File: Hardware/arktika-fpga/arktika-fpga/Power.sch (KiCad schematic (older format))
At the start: 40 parts

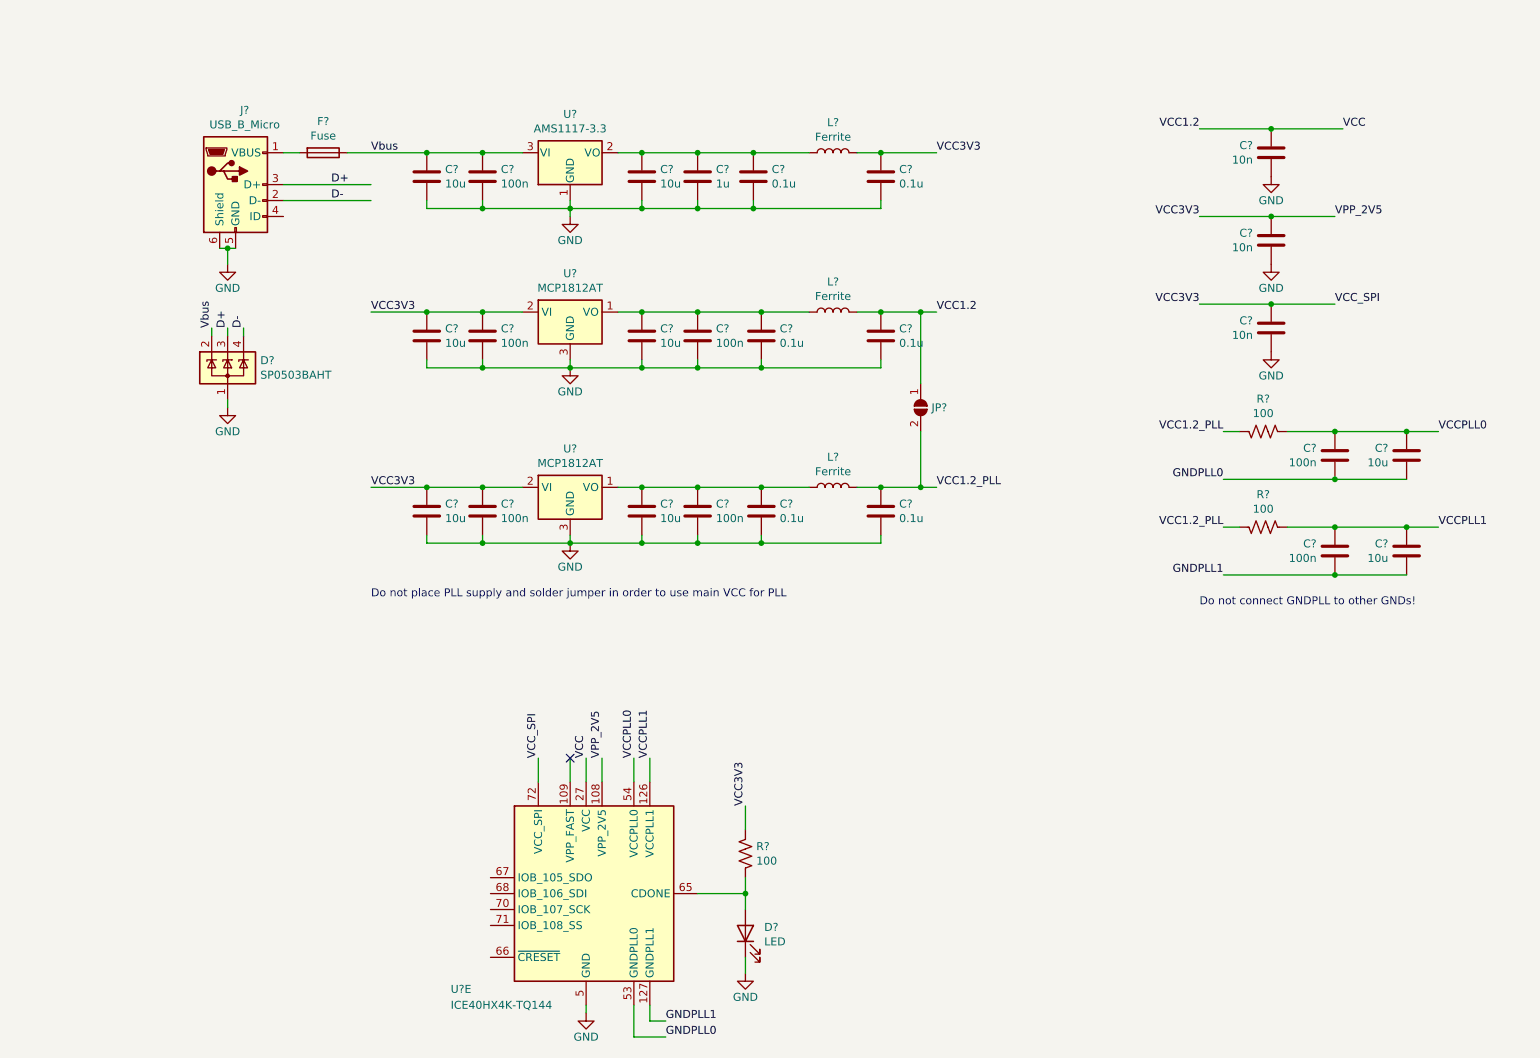
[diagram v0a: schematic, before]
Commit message: Started doing usb and programming
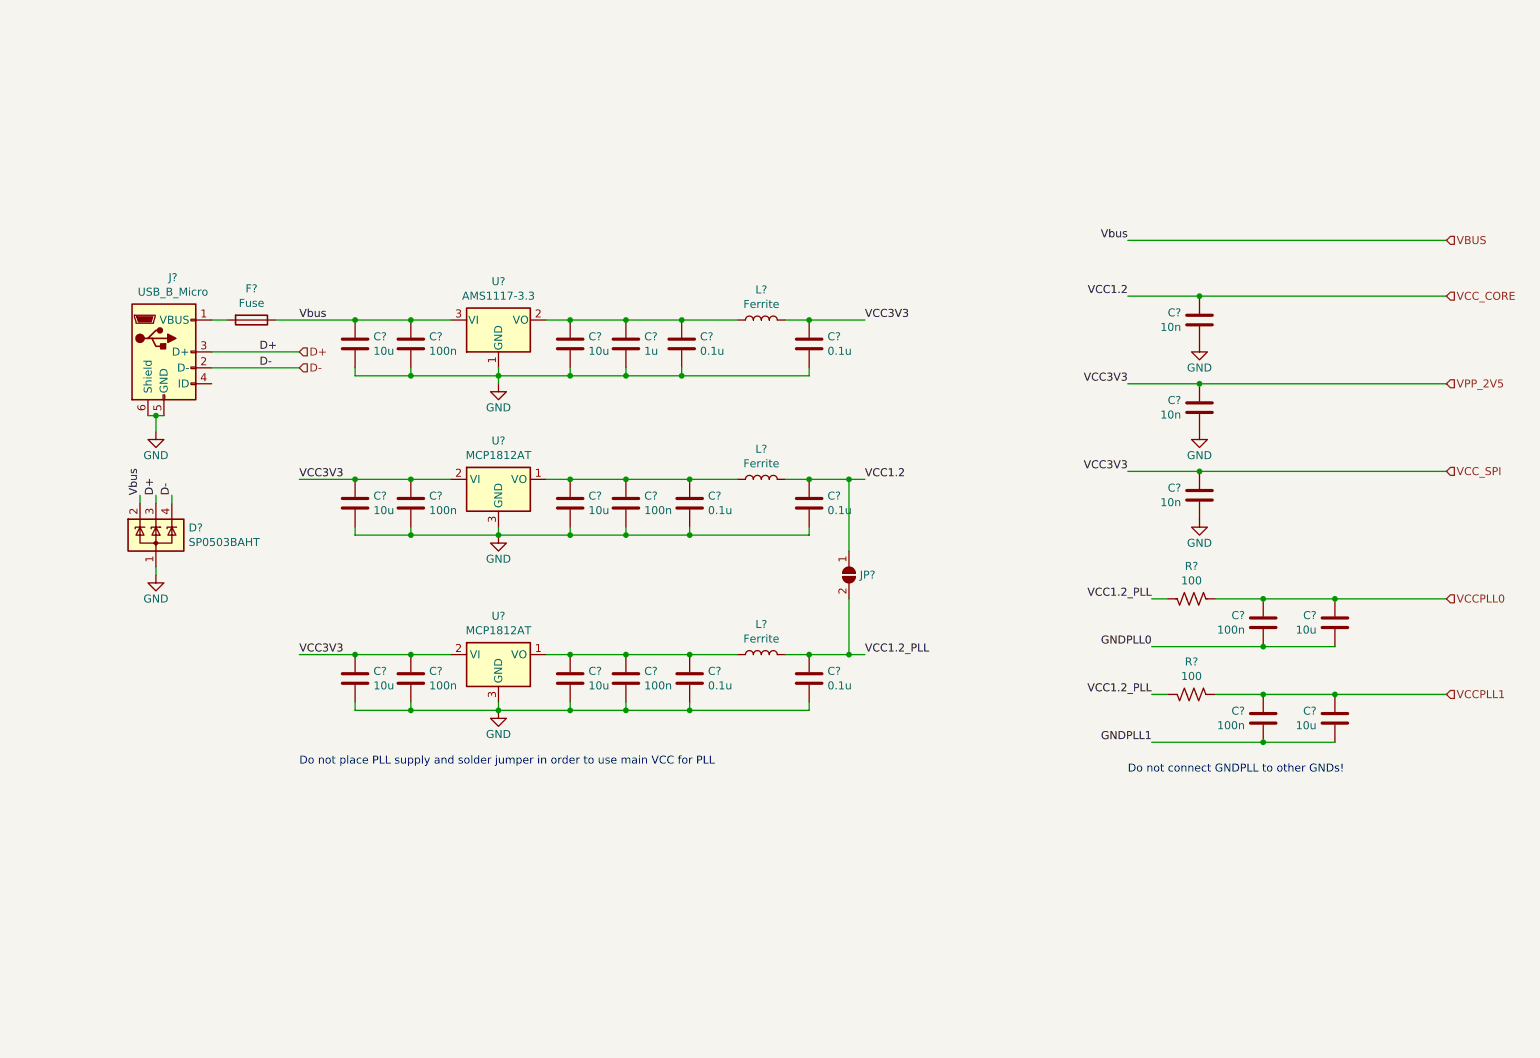
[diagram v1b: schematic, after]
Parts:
- removed D?: LED, symbol Device:LED
- removed R?: 100, symbol Device:R_US
- removed U?: ICE40HX4K-TQ144, Package_QFP:TQFP-144_20x20mm_P0.5mm, symbol FPGA_Lattice:ICE40HX4K-TQ144
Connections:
- net VCC renamed VCC_CORE
- net VCC3V3 renamed VCC_SPI
- net Vbus renamed VBUS
- no-connect marks 1 -> 0
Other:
- moved on the sheet: C?, D?, F?, J?, JP?, L?, R?, U?

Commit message: Added designators, some io, and some peripherals
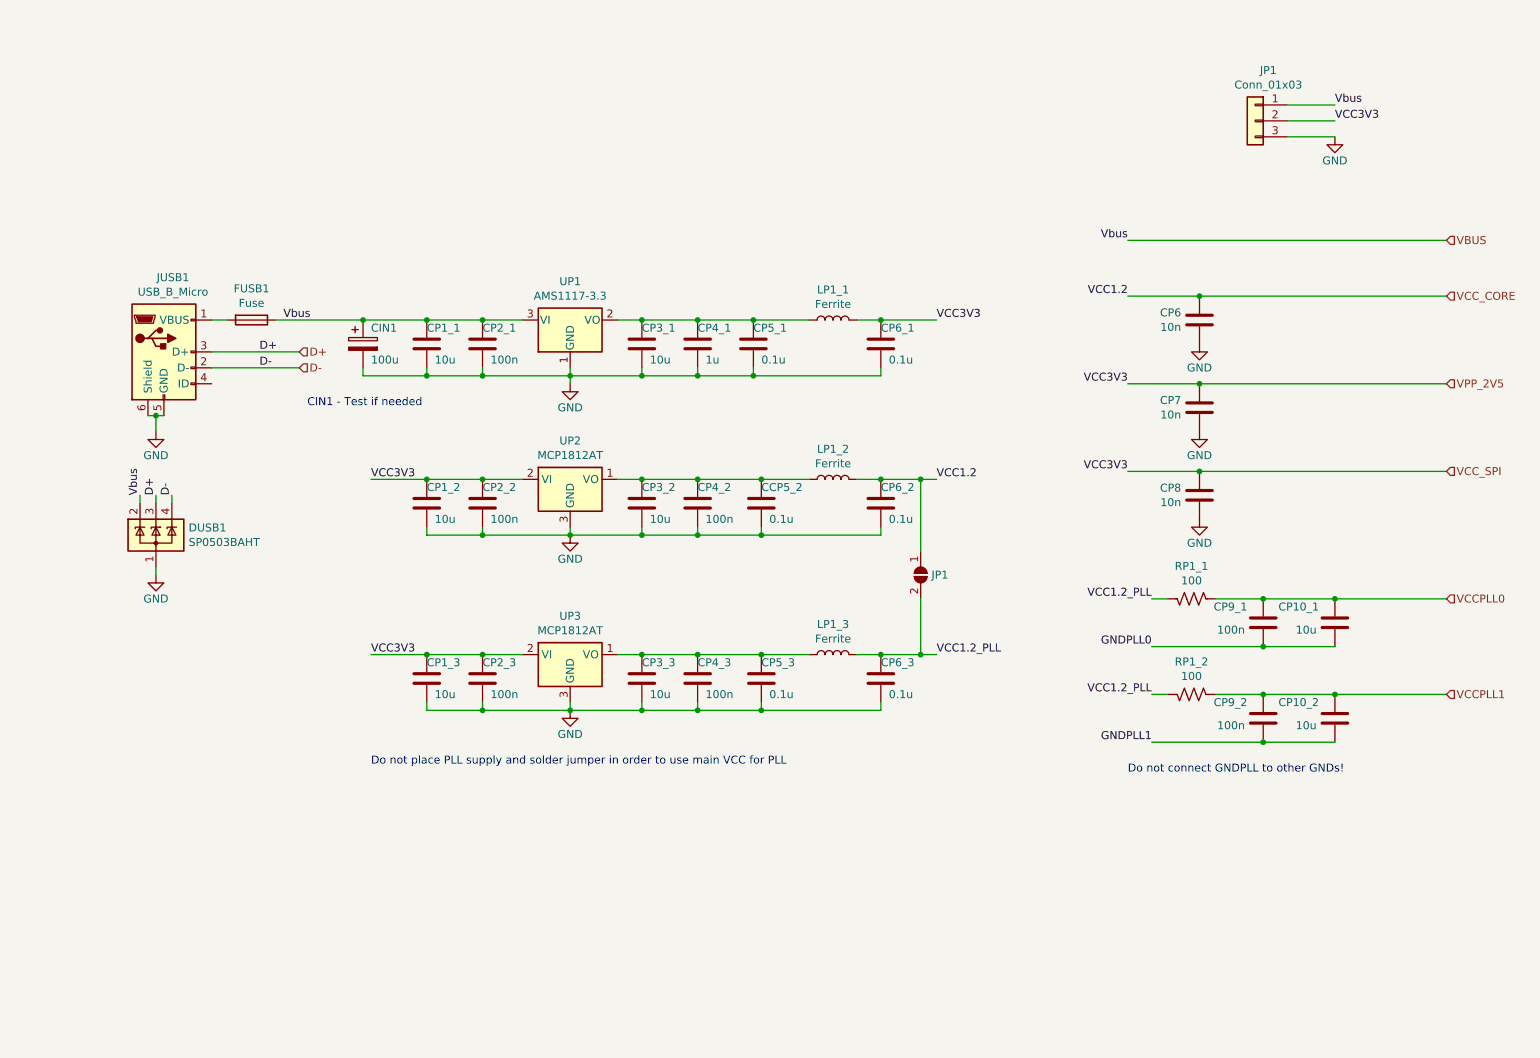
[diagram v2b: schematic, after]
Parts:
- added CIN1: 100u, symbol Device:CP
- added JP1: Conn_01x03, symbol Connector_Generic:Conn_01x03
- gave numbers to parts that had none: 37
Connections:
- net GND: now also CIN1.2, JP1.3 (Pin_3)
- net VBUS: now also CIN1.1, JP1.1 (Pin_1)
- net VCC_SPI: now also JP1.2 (Pin_2)
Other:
- note added: "CIN1 - Test if needed\n"
- moved on the sheet: CCP5_2, CP1_1, CP1_2, CP1_3, CP2_1, CP2_2, CP2_3, CP3_1, CP3_2, CP3_3, CP4_1, CP4_2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

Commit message: Assigned some footprints to components
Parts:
- CCP5_2, CIN1, CP10_1, CP10_2, CP1_1, CP1_2, CP1_3, CP2_1, CP2_2, CP2_3, CP3_1, CP3_2, CP3_3, CP4_1, CP4_2, CP4_3, CP5_1, CP5_3, CP6, CP6_1, CP6_2, CP6_3, CP7, CP8, CP9_1, CP9_2: footprint (none) -> Capacitors_SMD:C_0603
- JUSB1: footprint (none) -> Connectors:USB_Micro-B
- RP1_1, RP1_2: footprint (none) -> Resistors_SMD:R_0603
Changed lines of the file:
@@
 F 0 "CP3_2" H 4750 3750 50  0000 L CNN
 F 1 "10u" H 4800 3550 50  0000 L CNN
-F 2 "" H 4788 3500 50  0001 C CNN
+F 2 "Capacitors_SMD:C_0603" H 4788 3500 50  0001 C CNN
 F 3 "~" H 4750 3650 50  0001 C CNN
 	1    4750 3650
@@
 F 0 "CP4_2" H 5100 3750 50  0000 L CNN
 F 1 "100n" H 5150 3550 50  0000 L CNN
-F 2 "" H 5138 3500 50  0001 C CNN
+F 2 "Capacitors_SMD:C_0603" H 5138 3500 50  0001 C CNN
 F 3 "~" H 5100 3650 50  0001 C CNN
 	1    5100 3650
@@
 F 0 "CP1_2" H 3400 3750 50  0000 L CNN
 F 1 "10u" H 3450 3550 50  0000 L CNN
-F 2 "" H 3438 3500 50  0001 C CNN
+F 2 "Capacitors_SMD:C_0603" H 3438 3500 50  0001 C CNN
 F 3 "~" H 3400 3650 50  0001 C CNN
 	1    3400 3650
@@
 F 0 "CP2_2" H 3750 3750 50  0000 L CNN
 F 1 "100n" H 3800 3550 50  0000 L CNN
-F 2 "" H 3788 3500 50  0001 C CNN
+F 2 "Capacitors_SMD:C_0603" H 3788 3500 50  0001 C CNN
 F 3 "~" H 3750 3650 50  0001 C CNN
 	1    3750 3650
@@
 F 0 "CP3_3" H 4750 4850 50  0000 L CNN
 F 1 "10u" H 4800 4650 50  0000 L CNN
-F 2 "" H 4788 4600 50  0001 C CNN
+F 2 "Capacitors_SMD:C_0603" H 4788 4600 50  0001 C CNN
 F 3 "~" H 4750 4750 50  0001 C CNN
 	1    4750 4750
@@
 F 0 "CP4_3" H 5100 4850 50  0000 L CNN
 F 1 "100n" H 5150 4650 50  0000 L CNN
-F 2 "" H 5138 4600 50  0001 C CNN
+F 2 "Capacitors_SMD:C_0603" H 5138 4600 50  0001 C CNN
 F 3 "~" H 5100 4750 50  0001 C CNN
 	1    5100 4750
@@
 F 0 "CP1_3" H 3400 4850 50  0000 L CNN
 F 1 "10u" H 3450 4650 50  0000 L CNN
-F 2 "" H 3438 4600 50  0001 C CNN
+F 2 "Capacitors_SMD:C_0603" H 3438 4600 50  0001 C CNN
 F 3 "~" H 3400 4750 50  0001 C CNN
 	1    3400 4750
@@
 F 0 "CP2_3" H 3750 4850 50  0000 L CNN
 F 1 "100n" H 3800 4650 50  0000 L CNN
-F 2 "" H 3788 4600 50  0001 C CNN
+F 2 "Capacitors_SMD:C_0603" H 3788 4600 50  0001 C CNN
 F 3 "~" H 3750 4750 50  0001 C CNN
 	1    3750 4750
@@
 F 0 "RP1_2" V 7995 4850 50  0000 C CNN
 F 1 "100" V 8086 4850 50  0000 C CNN
-F 2 "" V 8240 4840 50  0001 C CNN
+F 2 "Resistors_SMD:R_0603" V 8240 4840 50  0001 C CNN
 F 3 "~" H 8200 4850 50  0001 C CNN
 	1    8200 4850
@@
 F 0 "CP10_2" H 9200 5100 50  0000 L CNN
 F 1 "10u" H 9215 4955 50  0000 L CNN
-F 2 "" H 9138 4850 50  0001 C CNN
+F 2 "Capacitors_SMD:C_0603" H 9138 4850 50  0001 C CNN
 F 3 "~" H 9100 5000 50  0001 C CNN
 	1    9100 5000
@@
 F 0 "CP9_2" H 8750 5100 50  0000 L CNN
 F 1 "100n" H 8765 4955 50  0000 L CNN
-F 2 "" H 8688 4850 50  0001 C CNN
+F 2 "Capacitors_SMD:C_0603" H 8688 4850 50  0001 C CNN
 F 3 "~" H 8650 5000 50  0001 C CNN
 	1    8650 5000
@@
 F 0 "RP1_1" V 7995 4250 50  0000 C CNN
 F 1 "100" V 8086 4250 50  0000 C CNN
-F 2 "" V 8240 4240 50  0001 C CNN
+F 2 "Resistors_SMD:R_0603" V 8240 4240 50  0001 C CNN
 F 3 "~" H 8200 4250 50  0001 C CNN
 	1    8200 4250
@@
 F 0 "CP10_1" H 9200 4500 50  0000 L CNN
 F 1 "10u" H 9215 4355 50  0000 L CNN
-F 2 "" H 9138 4250 50  0001 C CNN
+F 2 "Capacitors_SMD:C_0603" H 9138 4250 50  0001 C CNN
 F 3 "~" H 9100 4400 50  0001 C CNN
 	1    9100 4400
@@
 F 0 "CP9_1" H 8750 4500 50  0000 L CNN
 F 1 "100n" H 8765 4355 50  0000 L CNN
-F 2 "" H 8688 4250 50  0001 C CNN
+F 2 "Capacitors_SMD:C_0603" H 8688 4250 50  0001 C CNN
 F 3 "~" H 8650 4400 50  0001 C CNN
 	1    8650 4400
@@
 F 0 "CP4_1" H 5100 2750 50  0000 L CNN
 F 1 "1u" H 5150 2550 50  0000 L CNN
-F 2 "" H 5138 2500 50  0001 C CNN
+F 2 "Capacitors_SMD:C_0603" H 5138 2500 50  0001 C CNN
 F 3 "~" H 5100 2650 50  0001 C CNN
 	1    5100 2650
@@
 F 0 "CP3_1" H 4750 2750 50  0000 L CNN
 F 1 "10u" H 4800 2550 50  0000 L CNN
-F 2 "" H 4788 2500 50  0001 C CNN
+F 2 "Capacitors_SMD:C_0603" H 4788 2500 50  0001 C CNN
 F 3 "~" H 4750 2650 50  0001 C CNN
 	1    4750 2650
@@
 F 0 "CP2_1" H 3750 2750 50  0000 L CNN
 F 1 "100n" H 3800 2550 50  0000 L CNN
-F 2 "" H 3788 2500 50  0001 C CNN
+F 2 "Capacitors_SMD:C_0603" H 3788 2500 50  0001 C CNN
 F 3 "~" H 3750 2650 50  0001 C CNN
 	1    3750 2650
@@
 F 0 "CP1_1" H 3400 2750 50  0000 L CNN
 F 1 "10u" H 3450 2550 50  0000 L CNN
-F 2 "" H 3438 2500 50  0001 C CNN
+F 2 "Capacitors_SMD:C_0603" H 3438 2500 50  0001 C CNN
 F 3 "~" H 3400 2650 50  0001 C CNN
 	1    3400 2650
@@
 F 0 "JUSB1" H 1807 3167 50  0000 C CNN
 F 1 "USB_B_Micro" H 1807 3076 50  0000 C CNN
-F 2 "" H 1900 2650 50  0001 C CNN
+F 2 "Connectors:USB_Micro-B" H 1900 2650 50  0001 C CNN
 F 3 "~" H 1900 2650 50  0001 C CNN
 	1    1750 2700
@@
 F 0 "CP5_1" H 5450 2750 50  0000 L CNN
 F 1 "0.1u" H 5500 2550 50  0000 L CNN
-F 2 "" H 5488 2500 50  0001 C CNN
+F 2 "Capacitors_SMD:C_0603" H 5488 2500 50  0001 C CNN
 F 3 "~" H 5450 2650 50  0001 C CNN
 	1    5450 2650
@@
 F 0 "CCP5_2" H 5500 3750 50  0000 L CNN
 F 1 "0.1u" H 5550 3550 50  0000 L CNN
-F 2 "" H 5538 3500 50  0001 C CNN
+F 2 "Capacitors_SMD:C_0603" H 5538 3500 50  0001 C CNN
 F 3 "~" H 5500 3650 50  0001 C CNN
 	1    5500 3650
@@
 F 0 "CP5_3" H 5500 4850 50  0000 L CNN
 F 1 "0.1u" H 5550 4650 50  0000 L CNN
-F 2 "" H 5538 4600 50  0001 C CNN
+F 2 "Capacitors_SMD:C_0603" H 5538 4600 50  0001 C CNN
 F 3 "~" H 5500 4750 50  0001 C CNN
 	1    5500 4750
@@
 F 0 "CP6_1" H 6250 2750 50  0000 L CNN
 F 1 "0.1u" H 6300 2550 50  0000 L CNN
-F 2 "" H 6288 2500 50  0001 C CNN
+F 2 "Capacitors_SMD:C_0603" H 6288 2500 50  0001 C CNN
 F 3 "~" H 6250 2650 50  0001 C CNN
 	1    6250 2650
@@
 F 0 "CP6_2" H 6250 3750 50  0000 L CNN
 F 1 "0.1u" H 6300 3550 50  0000 L CNN
-F 2 "" H 6288 3500 50  0001 C CNN
+F 2 "Capacitors_SMD:C_0603" H 6288 3500 50  0001 C CNN
 F 3 "~" H 6250 3650 50  0001 C CNN
 	1    6250 3650
@@
 F 0 "CP6_3" H 6250 4850 50  0000 L CNN
 F 1 "0.1u" H 6300 4650 50  0000 L CNN
-F 2 "" H 6288 4600 50  0001 C CNN
+F 2 "Capacitors_SMD:C_0603" H 6288 4600 50  0001 C CNN
 F 3 "~" H 6250 4750 50  0001 C CNN
 	1    6250 4750
@@
 F 0 "CP8" H 8365 3646 50  0000 L CNN
 F 1 "10n" H 8365 3555 50  0000 L CNN
-F 2 "" H 8288 3450 50  0001 C CNN
+F 2 "Capacitors_SMD:C_0603" H 8288 3450 50  0001 C CNN
 F 3 "~" H 8250 3600 50  0001 C CNN
 	1    8250 3600
@@
 F 0 "CP7" H 8365 3096 50  0000 L CNN
 F 1 "10n" H 8365 3005 50  0000 L CNN
-F 2 "" H 8288 2900 50  0001 C CNN
+F 2 "Capacitors_SMD:C_0603" H 8288 2900 50  0001 C CNN
 F 3 "~" H 8250 3050 50  0001 C CNN
 	1    8250 3050
@@
 F 0 "CP6" H 8365 2546 50  0000 L CNN
 F 1 "10n" H 8365 2455 50  0000 L CNN
-F 2 "" H 8288 2350 50  0001 C CNN
+F 2 "Capacitors_SMD:C_0603" H 8288 2350 50  0001 C CNN
 F 3 "~" H 8250 2500 50  0001 C CNN
 	1    8250 2500
@@
 F 0 "CIN1" H 3050 2750 50  0000 L CNN
 F 1 "100u" H 3050 2550 50  0000 L CNN
-F 2 "" H 3038 2500 50  0001 C CNN
+F 2 "Capacitors_SMD:C_0603" H 3038 2500 50  0001 C CNN
 F 3 "~" H 3000 2650 50  0001 C CNN
 	1    3000 2650

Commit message: Minor fixes
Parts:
- CP4_2, CP4_3: value 100n -> 1u
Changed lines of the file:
@@
 AR Path="/5F3E98C5/5F40A16C" Ref="CP4_2"  Part="1"
 F 0 "CP4_2" H 5100 3750 50  0000 L CNN
-F 1 "100n" H 5150 3550 50  0000 L CNN
+F 1 "1u" H 5150 3550 50  0000 L CNN
 F 2 "Capacitors_SMD:C_0603" H 5138 3500 50  0001 C CNN
 F 3 "~" H 5100 3650 50  0001 C CNN
@@
 AR Path="/5F3E98C5/5F40A1BC" Ref="CP4_3"  Part="1"
 F 0 "CP4_3" H 5100 4850 50  0000 L CNN
-F 1 "100n" H 5150 4650 50  0000 L CNN
+F 1 "1u" H 5150 4650 50  0000 L CNN
 F 2 "Capacitors_SMD:C_0603" H 5138 4600 50  0001 C CNN
 F 3 "~" H 5100 4750 50  0001 C CNN
